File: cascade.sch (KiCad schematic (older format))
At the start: 12 parts, among them J1 Conn_01x01, J2 Conn_01x01, J3 Conn_01x01, J4 Conn_01x01

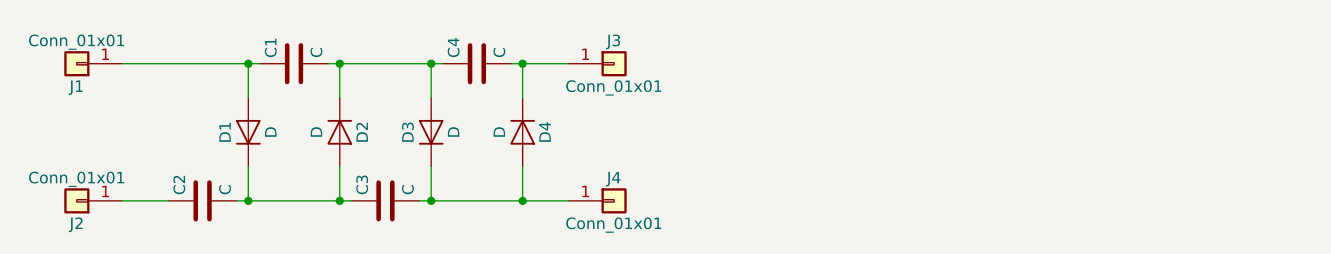
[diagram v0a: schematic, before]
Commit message: Move to new high density design
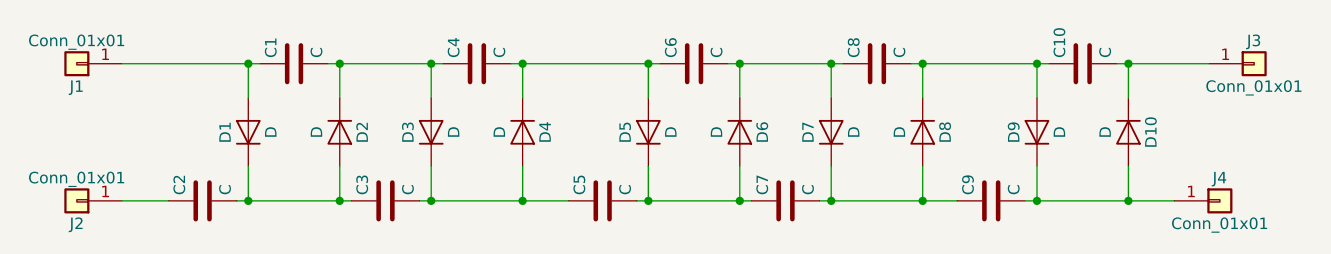
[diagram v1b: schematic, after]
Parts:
- added C10, C5, C6, C7, C8, C9: C, cascade:cap_20kv_10nf, symbol C
- added D10, D5, D6, D7, D8, D9: D, cascade:diode_2CL2FM, symbol D
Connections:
- net at C3.2, D3.1 (K), D4.2 (A): now also C5.1; no longer J4.1 (Pin_1)
- net at C4.2, D4.1 (K): now also C6.1, D5.2 (A); no longer J3.1 (Pin_1)
- new net: C10.2, D10.1 (K), J3.1 (Pin_1)
- new net: C9.2, D10.2 (A), D9.1 (K), J4.1 (Pin_1)
- new net: C6.2, C8.1, D6.1 (K), D7.2 (A)
- new net: C5.2, C7.1, D5.1 (K), D6.2 (A)
- new net: C7.2, C9.1, D7.1 (K), D8.2 (A)
- new net: C10.1, C8.2, D8.1 (K), D9.2 (A)
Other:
- moved on the sheet: J3, J4
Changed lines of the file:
@@
 LIBS:contrib
 LIBS:valves
+LIBS:cascade-cache
 EELAYER 25 0
 EELAYER END
@@
 	3150 2800 3150 2650
 Wire Wire Line
-	3100 2650 3350 2650
-Wire Wire Line
-	3150 3100 3150 3250
+	3150 3250 3150 3100
 Wire Wire Line
 	2700 3250 3350 3250
@@
 Connection ~ 2350 2650
 Wire Wire Line
-	2350 3100 2350 3250
+	2350 3250 2350 3100
 Wire Wire Line
 	1900 3250 2400 3250
@@
 L Conn_01x01 J3
 U 1 1 5B1B0D26
-P 3550 2650
-F 0 "J3" H 3550 2750 50  0000 C CNN
-F 1 "Conn_01x01" H 3550 2550 50  0000 C CNN
-F 2 "cascade:hv_pad" H 3550 2650 50  0001 C CNN
-F 3 "" H 3550 2650 50  0001 C CNN
-	1    3550 2650
+P 6350 2650
+F 0 "J3" H 6350 2750 50  0000 C CNN
+F 1 "Conn_01x01" H 6350 2550 50  0000 C CNN
+F 2 "cascade:hv_pad" H 6350 2650 50  0001 C CNN
+F 3 "" H 6350 2650 50  0001 C CNN
+	1    6350 2650
 	1    0    0    -1
 $EndComp
@@
 L Conn_01x01 J4
 U 1 1 5B1B0D81
-P 3550 3250
-F 0 "J4" H 3550 3350 50  0000 C CNN
-F 1 "Conn_01x01" H 3550 3150 50  0000 C CNN
-F 2 "cascade:hv_pad" H 3550 3250 50  0001 C CNN
-F 3 "" H 3550 3250 50  0001 C CNN
-	1    3550 3250
+P 6200 3250
+F 0 "J4" H 6200 3350 50  0000 C CNN
+F 1 "Conn_01x01" H 6200 3150 50  0000 C CNN
+F 2 "cascade:hv_pad" H 6200 3250 50  0001 C CNN
+F 3 "" H 6200 3250 50  0001 C CNN
+	1    6200 3250
 	1    0    0    -1
 $EndComp
+Wire Wire Line
+	3100 2650 3750 2650
+$Comp
+L C C6
+U 1 1 5B1B5460
+P 3900 2650
+F 0 "C6" H 3925 2750 50  0000 L CNN
+F 1 "C" H 3925 2550 50  0000 L CNN
+F 2 "cascade:cap_20kv_10nf" H 3938 2500 50  0001 C CNN
+F 3 "" H 3900 2650 50  0001 C CNN
+	1    3900 2650
+	0    -1   -1   0
+$EndComp
+$Comp
+L D D5
+U 1 1 5B1B5466
+P 3700 2950
+F 0 "D5" H 3700 3050 50  0000 C CNN
+F 1 "D" H 3700 2850 50  0000 C CNN
+F 2 "cascade:diode_2CL2FM" H 3700 2950 50  0001 C CNN
+F 3 "" H 3700 2950 50  0001 C CNN
+	1    3700 2950
+	0    -1   -1   0
+$EndComp
+$Comp
+L C C5
+U 1 1 5B1B546C
+P 3500 3250
+F 0 "C5" H 3525 3350 50  0000 L CNN
+F 1 "C" H 3525 3150 50  0000 L CNN
+F 2 "cascade:cap_20kv_10nf" H 3538 3100 50  0001 C CNN
+F 3 "" H 3500 3250 50  0001 C CNN
+	1    3500 3250
+	0    -1   -1   0
+$EndComp
+$Comp
+L C C7
+U 1 1 5B1B5472
+P 4300 3250
+F 0 "C7" H 4325 3350 50  0000 L CNN
+F 1 "C" H 4325 3150 50  0000 L CNN
+F 2 "cascade:cap_20kv_10nf" H 4338 3100 50  0001 C CNN
+F 3 "" H 4300 3250 50  0001 C CNN
+	1    4300 3250
+	0    -1   -1   0
+$EndComp
+$Comp
+L C C8
+U 1 1 5B1B5478
+P 4700 2650
+F 0 "C8" H 4725 2750 50  0000 L CNN
+F 1 "C" H 4725 2550 50  0000 L CNN
+F 2 "cascade:cap_20kv_10nf" H 4738 2500 50  0001 C CNN
+F 3 "" H 4700 2650 50  0001 C CNN
+	1    4700 2650
+	0    -1   -1   0
+$EndComp
+Wire Wire Line
+	4050 2650 4550 2650
+Wire Wire Line
+	4900 2800 4900 2650
+Wire Wire Line
+	4900 3250 4900 3100
+Wire Wire Line
+	4450 3250 5050 3250
+Wire Wire Line
+	4500 3100 4500 3250
+Connection ~ 4500 3250
+Wire Wire Line
+	4500 2800 4500 2650
+Connection ~ 4500 2650
+Wire Wire Line
+	4100 2800 4100 2650
+Connection ~ 4100 2650
+Wire Wire Line
+	4100 3250 4100 3100
+Wire Wire Line
+	3650 3250 4150 3250
+Connection ~ 4100 3250
+Wire Wire Line
+	3700 3100 3700 3250
+Connection ~ 3700 3250
+Wire Wire Line
+	3700 2800 3700 2650
+Connection ~ 4900 3250
+Connection ~ 4900 2650
+Connection ~ 3700 2650
+$Comp
+L D D6
+U 1 1 5B1B5493
+P 4100 2950
+F 0 "D6" H 4100 3050 50  0000 C CNN
+F 1 "D" H 4100 2850 50  0000 C CNN
+F 2 "cascade:diode_2CL2FM" H 4100 2950 50  0001 C CNN
+F 3 "" H 4100 2950 50  0001 C CNN
+	1    4100 2950
+	0    1    1    0
+$EndComp
+$Comp
+L D D7
+U 1 1 5B1B5499
+P 4500 2950
+F 0 "D7" H 4500 3050 50  0000 C CNN
+F 1 "D" H 4500 2850 50  0000 C CNN
+F 2 "cascade:diode_2CL2FM" H 4500 2950 50  0001 C CNN
+F 3 "" H 4500 2950 50  0001 C CNN
+	1    4500 2950
+	0    -1   -1   0
+$EndComp
+$Comp
+L D D8
+U 1 1 5B1B549F
+P 4900 2950
+F 0 "D8" H 4900 3050 50  0000 C CNN
+F 1 "D" H 4900 2850 50  0000 C CNN
+F 2 "cascade:diode_2CL2FM" H 4900 2950 50  0001 C CNN
+F 3 "" H 4900 2950 50  0001 C CNN
+	1    4900 2950
+	0    1    1    0
+$EndComp
+Wire Wire Line
+	4850 2650 5450 2650
+$Comp
+L C C9
+U 1 1 5B1B5EC7
+P 5200 3250
+F 0 "C9" H 5225 3350 50  0000 L CNN
+F 1 "C" H 5225 3150 50  0000 L CNN
+F 2 "cascade:cap_20kv_10nf" H 5238 3100 50  0001 C CNN
+F 3 "" H 5200 3250 50  0001 C CNN
+	1    5200 3250
+	0    -1   -1   0
+$EndComp
+$Comp
+L C C10
+U 1 1 5B1B5ECD
+P 5600 2650
+F 0 "C10" H 5625 2750 50  0000 L CNN
+F 1 "C" H 5625 2550 50  0000 L CNN
+F 2 "cascade:cap_20kv_10nf" H 5638 2500 50  0001 C CNN
+F 3 "" H 5600 2650 50  0001 C CNN
+	1    5600 2650
+	0    -1   -1   0
+$EndComp
+Wire Wire Line
+	5800 2800 5800 2650
+Wire Wire Line
+	5800 3250 5800 3100
+Wire Wire Line
+	5350 3250 6000 3250
+Wire Wire Line
+	5400 3100 5400 3250
+Connection ~ 5400 3250
+Wire Wire Line
+	5400 2800 5400 2650
+Connection ~ 5400 2650
+Connection ~ 5800 3250
+Connection ~ 5800 2650
+$Comp
+L D D9
+U 1 1 5B1B5EE0
+P 5400 2950
+F 0 "D9" H 5400 3050 50  0000 C CNN
+F 1 "D" H 5400 2850 50  0000 C CNN
+F 2 "cascade:diode_2CL2FM" H 5400 2950 50  0001 C CNN
+F 3 "" H 5400 2950 50  0001 C CNN
+	1    5400 2950
+	0    -1   -1   0
+$EndComp
+$Comp
+L D D10
+U 1 1 5B1B5EE6
+P 5800 2950
+F 0 "D10" H 5800 3050 50  0000 C CNN
+F 1 "D" H 5800 2850 50  0000 C CNN
+F 2 "cascade:diode_2CL2FM" H 5800 2950 50  0001 C CNN
+F 3 "" H 5800 2950 50  0001 C CNN
+	1    5800 2950
+	0    1    1    0
+$EndComp
+Wire Wire Line
+	5750 2650 6150 2650
 $EndSCHEMATC
